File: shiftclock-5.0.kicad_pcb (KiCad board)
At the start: 4 copper layers, 131.9 x 27.5 mm, 37 parts, among them J1 USB_C_Receptacle_USB2.0_16P, SW1 SW1, SW2 SW2, SW3 SW3 / BOOT, SW4 RotaryEncoder_Switch, SW5 RESET, U1 CC56-12SURKWA, U2 CC56-12SURKWA, U3 MAX7219, U5 CH340C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

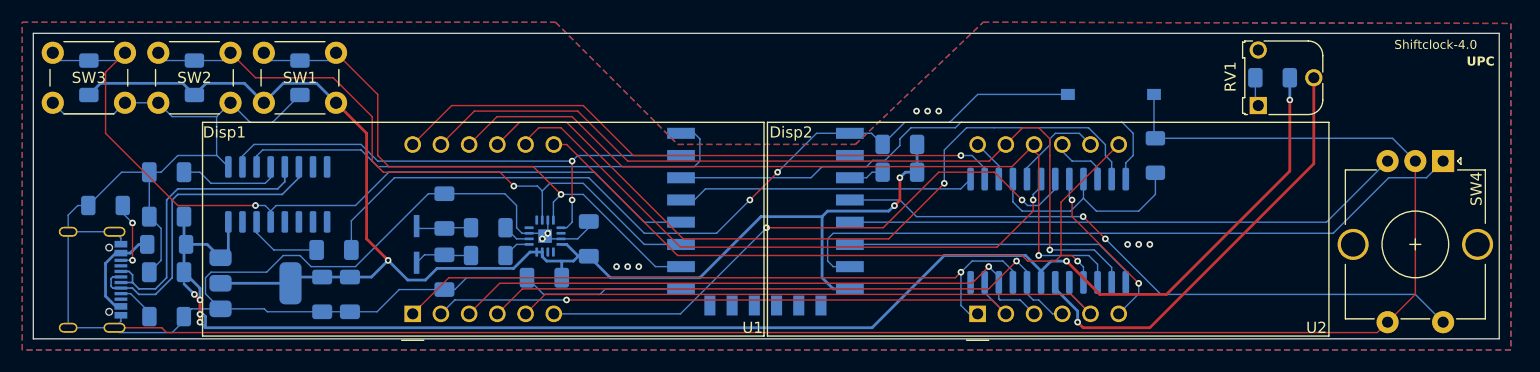
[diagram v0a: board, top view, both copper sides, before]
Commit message: Rework Schematic and Begin Layout Connections
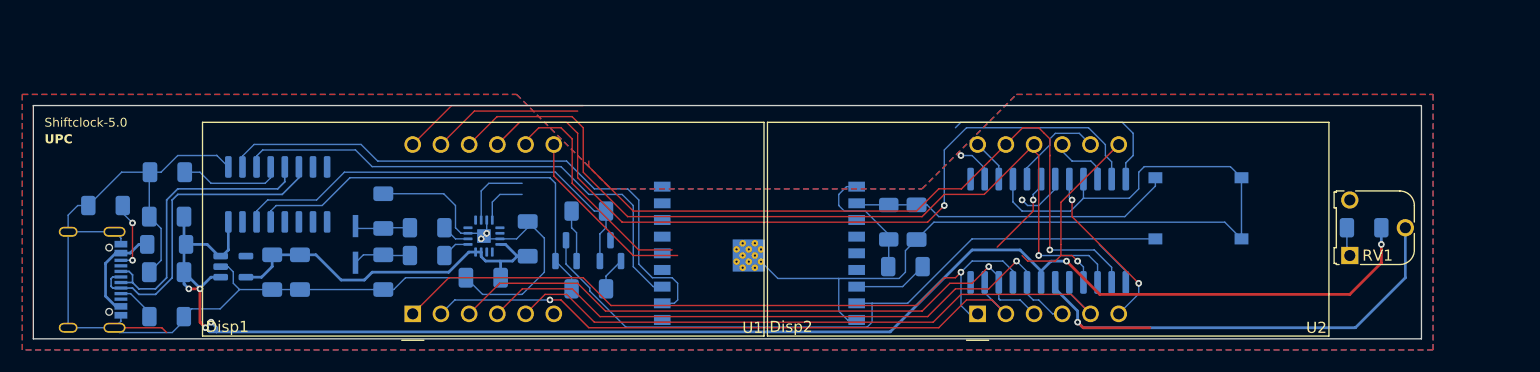
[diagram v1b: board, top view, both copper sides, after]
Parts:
- removed C1, C4: 100nF, Capacitor_SMD:C_1206_3216Metric_Pad1.33x1.80mm_HandSolder
- removed R2, R3, R4, R5, R6: 10K, Resistor_SMD:R_1206_3216Metric_Pad1.30x1.75mm_HandSolder
- removed R9: 150, Resistor_SMD:R_1206_3216Metric_Pad1.30x1.75mm_HandSolder
- removed SW1: SW1, Button_Switch_THT:SW_PUSH_6mm_H5mm
- removed SW2: SW2, Button_Switch_THT:SW_PUSH_6mm_H5mm
- removed SW3: SW3 / BOOT, Button_Switch_THT:SW_PUSH_6mm_H5mm
- removed SW4: RotaryEncoder_Switch, Rotary_Encoder:RotaryEncoder_Alps_EC12E-Switch_Vertical_H20mm_CircularMountingHoles
- removed SW5: RESET, Button_Switch_SMD:SW_Tactile_SPST_NO_Straight_CK_PTS636Sx25SMTRLFS
- removed U6: AMS1117-3.3, Package_TO_SOT_SMD:SOT-223-3_TabPin2
- removed U7: ESP-12F, RF_Module:ESP-12E
- added C11: 1uF, Capacitor_SMD:C_1206_3216Metric_Pad1.33x1.80mm_HandSolder, B.Cu at (102.5, 56.0)
- added C12: 100nF, Capacitor_SMD:C_1206_3216Metric_Pad1.33x1.80mm_HandSolder, B.Cu at (35.1, 51.5)
- added Q1: SS8050, Package_TO_SOT_SMD:SOT-23, B.Cu at (75.0, 58.6)
- added Q2: SS8050, Package_TO_SOT_SMD:SOT-23, B.Cu at (71.0, 58.6)
- added R10: 10K, Resistor_SMD:R_1206_3216Metric_Pad1.30x1.75mm_HandSolder, B.Cu at (100.0, 56.0)
- added R11: 10K, Resistor_SMD:R_1206_3216Metric_Pad1.30x1.75mm_HandSolder, B.Cu at (101.5, 60.0)
- added R12: 10K, Resistor_SMD:R_1206_3216Metric_Pad1.30x1.75mm_HandSolder, B.Cu at (73.0, 55.0)
- added R13: 10K, Resistor_SMD:R_1206_3216Metric_Pad1.30x1.75mm_HandSolder, B.Cu at (73.0, 62.0)
- added SW6: RESET, Button_Switch_SMD:SW_Tactile_SPST_NO_Straight_CK_PTS636Sx25SMTRLFS, B.Cu at (127.9, 52.0)
- added SW7: BOOT, Button_Switch_SMD:SW_Tactile_SPST_NO_Straight_CK_PTS636Sx25SMTRLFS, B.Cu at (127.9, 57.5)
- added U4: ESP32-C3-WROOM-02, RF_Module:ESP32-C3-WROOM-02, B.Cu at (88.4, 58.8)
- added U9: CH340C, Package_SO:SOIC-16_3.9x9.9mm_P1.27mm, B.Cu at (45.0, 53.5)
- U5: value CH340C -> ME6211C33M5; footprint Package_SO:SOIC-16_3.9x9.9mm_P1.27mm -> Package_TO_SOT_SMD:SOT-23-5
- moved RV1 15.8 mm to (141.5, 59.0)
- moved R1 15.8 mm to (142.8, 56.5)
- moved U5 7.63 mm to (41.0, 60.0), turned to 0 degrees
- moved C10 5.50 mm to (54.5, 60.5)
- moved C5 5.50 mm to (63.5, 61.0)
- moved C6 5.50 mm to (67.5, 57.5)
- moved C9 5.50 mm to (54.5, 55.0)
- moved FB1 5.50 mm to (58.5, 56.5)
- moved FB2 5.50 mm to (58.5, 59.0)
- moved LS1 5.50 mm to (52.0, 58.0)
- moved U8 5.50 mm to (63.6, 57.2)
- moved C2 4.92 mm to (44.5, 60.5)
- moved C8 4.92 mm to (47.0, 60.5)
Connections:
- U3 pad 1: DIN -> IO7
- U3 pad 12: LOAD -> IO10
- U3 pad 13: CLK -> IO6
- U3 pad 4: Net-(R9-Pad1) -> GND
- U3 pad 9: Net-(R9-Pad1) -> GND
- U5 pad 1: GND -> VCC
- U5 pad 2: TX -> GND
- U5 pad 3: RX -> VCC
- U5 pad 4: Net-(U5-V3) -> unconnected-(U5-NC-Pad4)
- U5 pad 5: D+ -> 3.3V
- U8 pad 1: TX -> IO3
- U8 pad 14: IO2 -> IO5
- U8 pad 16: IO15 -> IO4
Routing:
- net GND: track 337.1 -> 207.1 mm, vias 11 -> 2
- net 3.3V: track 128.2 -> 44.4 mm, vias 3 -> 0
- net RESET: track 76.8 -> 0.00 mm, vias 2 -> 0
- net IO0: track 74.0 -> 0.00 mm, vias 1 -> 0
- net IO9: track 0.00 -> 63.4 mm
- net ENC1: track 62.5 -> 0.00 mm
- net IO2: track 60.3 -> 0.00 mm, vias 1 -> 0
- net ENC3: track 58.0 -> 0.00 mm, vias 2 -> 0
- net IO15: track 51.9 -> 0.00 mm, vias 1 -> 0
- net ENC2: track 50.7 -> 0.00 mm
- net DIG3: track 53.2 -> 4.70 mm, vias 2 -> 1
- net LOAD: track 47.9 -> 0.00 mm
- net RTS: track 0.00 -> 40.1 mm
- net DTR: track 0.00 -> 38.2 mm
- net DIG0: track 56.3 -> 20.4 mm
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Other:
- board size 131.9 x 27.5 mm -> 124.9 x 21 mm
- board text added: "Shiftclock-5.0"
- board text removed: "Shiftclock-4.0"

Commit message: Add Netlist
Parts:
- added R2: 10K, Resistor_SMD:R_1206_3216Metric_Pad1.30x1.75mm_HandSolder, B.Cu at (102.5, 61.0)
- added TP1: TestPoint, TestPoint:TestPoint_Pad_2.0x2.0mm, B.Cu at (45.5, 64.5)
- added TP2: TestPoint, TestPoint:TestPoint_Pad_2.0x2.0mm, B.Cu at (50.7, 63.5)
- added TP3: TestPoint, TestPoint:TestPoint_Pad_2.0x2.0mm, B.Cu at (41.5, 63.5)
- added TP4: TestPoint, TestPoint:TestPoint_Pad_2.0x2.0mm, B.Cu at (53.0, 49.0)
- added TP5: TestPoint, TestPoint:TestPoint_Pad_2.0x2.0mm, B.Cu at (77.0, 63.0)
- added TP6: TestPoint, TestPoint:TestPoint_Pad_2.0x2.0mm, B.Cu at (61.5, 53.5)
- added TP7: TestPoint, TestPoint:TestPoint_Pad_2.0x2.0mm, B.Cu at (69.0, 52.5)
- moved R11 1.80 mm to (100.0, 61.0), turned to -90 degrees
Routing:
- net DIG3: track 4.70 -> 72.5 mm
- net DIG0: track 20.4 -> 62.1 mm, vias 1 -> 3
- net 3.3V: track 44.4 -> 83.8 mm, vias 0 -> 2
- net IO10: track 21.0 -> 59.3 mm
- net IO4: track 4.60 -> 37.8 mm, vias 0 -> 2
- net IO5: track 6.60 -> 39.0 mm, vias 0 -> 2
- net B: track 36.9 -> 69.0 mm
- net GND: track 207.1 -> 235.3 mm, vias 2 -> 7
- net EN: track 29.3 -> 57.4 mm, vias 0 -> 2
- net DIG2: track 28.7 -> 56.7 mm
- net IO6: track 4.42 -> 26.6 mm, vias 0 -> 2
- net IO7: track 0.00 -> 22.0 mm, vias 0 -> 2
- net IO3: track 0.00 -> 20.4 mm, vias 0 -> 2
- net Net-(U3-ISET): track 47.2 -> 40.5 mm, vias 1 -> 0
- net A: track 78.3 -> 81.9 mm, vias 1 -> 3
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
